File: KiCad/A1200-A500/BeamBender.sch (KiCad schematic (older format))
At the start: 42 parts, among them J1 4-1734742-0, J2 HDMI_A_1.4, J3 STX-3501-3N, J4 Phoenix_Contact, U1 LM1117-3.3, U3 ADV7513BSWZ, X1 Abracon ASE-27.000MHZ-L-R-T

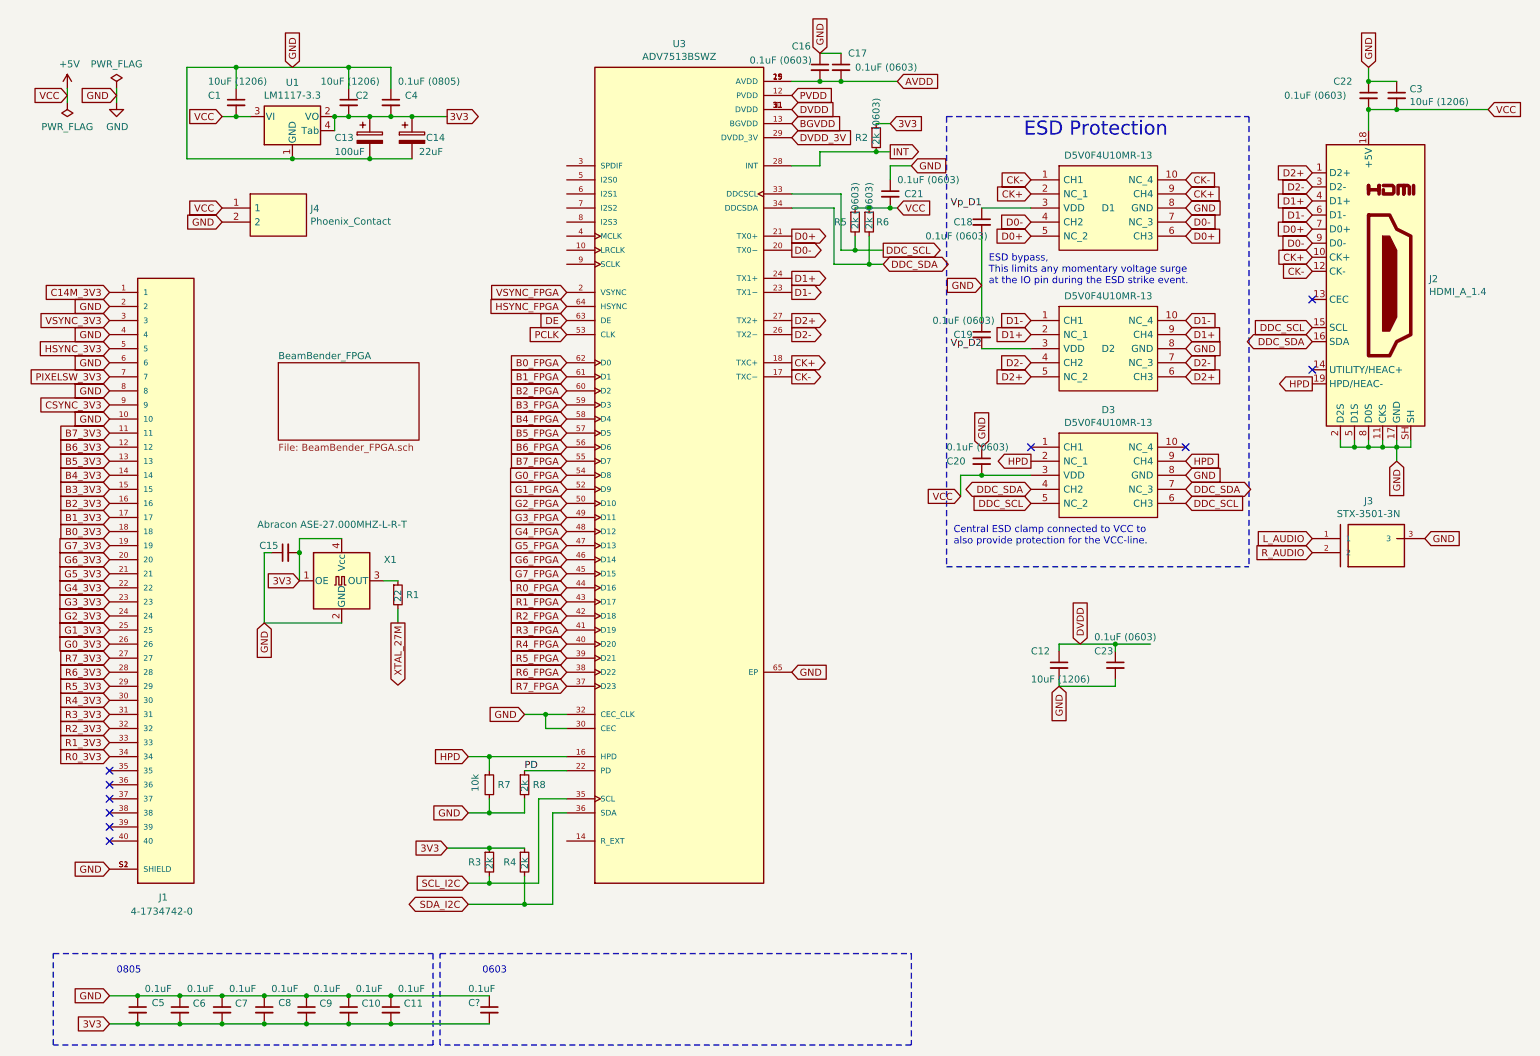
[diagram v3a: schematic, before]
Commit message: Added Oscillator_7.0x5.0mm X2 on GCLKT_1 input and added damping resistor on PCLK
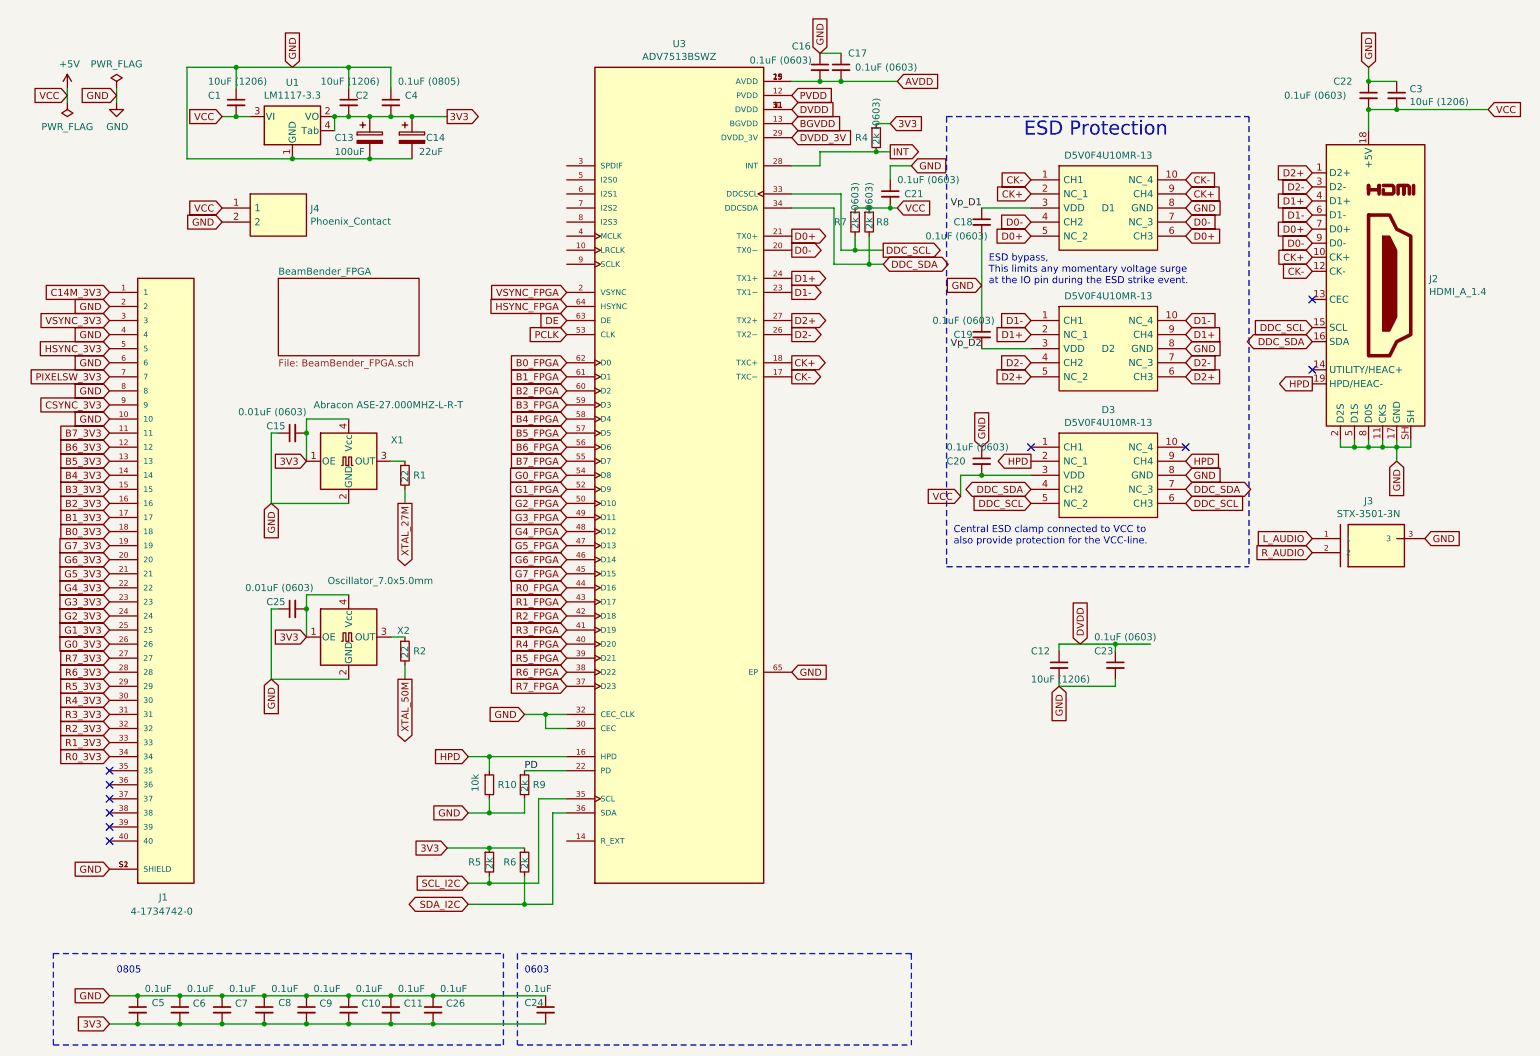
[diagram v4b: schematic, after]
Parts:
- added C25: 0.01uF (0603), Capacitor_SMD:C_0603_1608Metric_Pad1.08x0.95mm_HandSolder, symbol Device:C_Small
- added C26: 0.1uF, Capacitor_SMD:C_0805_2012Metric_Pad1.18x1.45mm_HandSolder, symbol Device:C_Small
- added R2: 22, Resistor_SMD:R_0603_1608Metric_Pad0.98x0.95mm_HandSolder, symbol Device:R_Small
- added X2: Oscillator_7.0x5.0mm, Oscillator:Oscillator_SMD_SeikoEpson_SG8002CA-4Pin_7.0x5.0mm_HandSoldering, symbol Oscillator:SG-8002CA
- C15: value 0.01uF -> 0.01uF (0603)
- C5, C8: footprint Capacitor_SMD:C_0805_2012Metric_Pad1.15x1.40mm_HandSolder -> Capacitor_SMD:C_0805_2012Metric_Pad1.18x1.45mm_HandSolder
- gave numbers to parts that had none: 1
- renumbered R7 to R10, R2 to R4, R3 to R5, R4 to R6, R5 to R7, R6 to R8, R8 to R9
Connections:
- net 3V3: now also C25.2, C26.2, X2.1 (OE), X2.4 (Vcc)
- net GND: now also C25.1, C26.1, X2.2 (GND)
- new net: R2.1, X2.3 (OUT)
- new net XTAL_50M: R2.2
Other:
- moved on the sheet: C15, C24, R1, X1
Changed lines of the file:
@@
 F 0 "C5" H 1450 7550 50  0000 L CNN
 F 1 "0.1uF" H 1400 7650 50  0000 L CNN
-F 2 "Capacitor_SMD:C_0805_2012Metric_Pad1.15x1.40mm_HandSolder" H 1350 7500 50  0001 C CNN
+F 2 "Capacitor_SMD:C_0805_2012Metric_Pad1.18x1.45mm_HandSolder" H 1350 7500 50  0001 C CNN
 F 3 "~" H 1350 7500 50  0001 C CNN
 	1    1350 7500
@@
 F 0 "C8" H 2350 7550 50  0000 L CNN
 F 1 "0.1uF" H 2300 7650 50  0000 L CNN
-F 2 "Capacitor_SMD:C_0805_2012Metric_Pad1.15x1.40mm_HandSolder" H 2250 7500 50  0001 C CNN
+F 2 "Capacitor_SMD:C_0805_2012Metric_Pad1.18x1.45mm_HandSolder" H 2250 7500 50  0001 C CNN
 F 3 "~" H 2250 7500 50  0001 C CNN
 	1    2250 7500
@@
 GND
 $Comp
-L Device:R_Small R5
+L Device:R_Small R7
 U 1 1 6532D8B1
 P 6450 1900
-F 0 "R5" H 6300 1900 50  0000 L CNN
+F 0 "R7" H 6300 1900 50  0000 L CNN
 F 1 "2k  (0603)" V 6450 1850 50  0000 L CNN
 F 2 "Resistor_SMD:R_0603_1608Metric_Pad0.98x0.95mm_HandSolder" H 6450 1900 50  0001 C CNN
@@
 Connection ~ 3000 1450
 $Sheet
-S 2350 2900 1000 550
+S 2350 2300 1000 550
 U 6541C824
 F0 "BeamBender_FPGA" 50
@@
 L Oscillator:SG-8002CE X1
 U 1 1 654B3E8F
-P 2800 4450
-F 0 "X1" H 3100 4600 50  0000 L CNN
-F 1 "Abracon ASE-27.000MHZ-L-R-T" H 2200 4850 50  0000 L CNN
-F 2 "Oscillator:Oscillator_SMD_SeikoEpson_SG8002CE-4Pin_3.2x2.5mm" H 3500 4100 50  0001 C CNN
-F 3 "https://www.mouser.com/datasheet/2/3/ASEseries-1774818.pdf" H 2700 4450 50  0001 C CNN
-	1    2800 4450
-	1    0    0    -1
-$EndComp
-Text GLabel 2250 4750 3    50   Input ~ 0
-GND
-Text GLabel 2500 4450 0    50   Input ~ 0
+P 2850 3600
+F 0 "X1" H 3150 3750 50  0000 L CNN
+F 1 "Abracon ASE-27.000MHZ-L-R-T" H 2600 4000 50  0000 L CNN
+F 2 "Oscillator:Oscillator_SMD_SeikoEpson_SG8002CE-4Pin_3.2x2.5mm" H 3550 3250 50  0001 C CNN
+F 3 "https://www.mouser.com/datasheet/2/3/ASEseries-1774818.pdf" H 2750 3600 50  0001 C CNN
+	1    2850 3600
+	1    0    0    -1
+$EndComp
+Text GLabel 2300 3900 3    50   Input ~ 0
+GND
+Text GLabel 2550 3600 0    50   Input ~ 0
 3V3
 Wire Wire Line
-	2500 4450 2500 4250
-Wire Wire Line
-	2500 4150 2800 4150
+	2550 3600 2550 3400
+Wire Wire Line
+	2550 3300 2850 3300
 $Comp
 L Device:C_Small C15
 U 1 1 654BAF9D
-P 2400 4250
-F 0 "C15" V 2450 4300 50  0000 L CNN
-F 1 "0.01uF" H 2492 4205 50  0001 L CNN
-F 2 "Capacitor_SMD:C_0603_1608Metric_Pad1.08x0.95mm_HandSolder" H 2400 4250 50  0001 C CNN
-F 3 "~" H 2400 4250 50  0001 C CNN
-	1    2400 4250
+P 2450 3400
+F 0 "C15" V 2500 3450 50  0000 L CNN
+F 1 "0.01uF (0603)" V 2600 3300 50  0000 L CNN
+F 2 "Capacitor_SMD:C_0603_1608Metric_Pad1.08x0.95mm_HandSolder" H 2450 3400 50  0001 C CNN
+F 3 "~" H 2450 3400 50  0001 C CNN
+	1    2450 3400
 	0    -1   -1   0
 $EndComp
-Connection ~ 2500 4250
-Wire Wire Line
-	2500 4250 2500 4150
-Wire Wire Line
-	2800 4750 2250 4750
-Wire Wire Line
-	2250 4750 2250 4250
-Wire Wire Line
-	2250 4250 2300 4250
-Text GLabel 3200 4750 3    50   Output ~ 0
+Connection ~ 2550 3400
+Wire Wire Line
+	2550 3400 2550 3300
+Wire Wire Line
+	2850 3900 2300 3900
+Wire Wire Line
+	2300 3900 2300 3400
+Wire Wire Line
+	2300 3400 2350 3400
+Text GLabel 3250 3900 3    50   Output ~ 0
 XTAL_27M
 $Comp
 L Device:R_Small R1
 U 1 1 65512C64
-P 3200 4550
-F 0 "R1" H 3259 4550 50  0000 L CNN
-F 1 "22" V 3200 4500 50  0000 L CNN
-F 2 "Resistor_SMD:R_0603_1608Metric_Pad0.98x0.95mm_HandSolder" H 3200 4550 50  0001 C CNN
-F 3 "~" H 3200 4550 50  0001 C CNN
-	1    3200 4550
-	1    0    0    -1
-$EndComp
-Wire Wire Line
-	3100 4450 3200 4450
-Wire Wire Line
-	3200 4650 3200 4750
+P 3250 3700
+F 0 "R1" H 3309 3700 50  0000 L CNN
+F 1 "22" V 3250 3650 50  0000 L CNN
+F 2 "Resistor_SMD:R_0603_1608Metric_Pad0.98x0.95mm_HandSolder" H 3250 3700 50  0001 C CNN
+F 3 "~" H 3250 3700 50  0001 C CNN
+	1    3250 3700
+	1    0    0    -1
+$EndComp
+Wire Wire Line
+	3150 3600 3250 3600
+Wire Wire Line
+	3250 3800 3250 3900
 Text GLabel 1150 7600 0    50   Input ~ 0
 3V3
@@
 Connection ~ 3300 1150
 $Comp
-L Device:R_Small R6
+L Device:R_Small R8
 U 1 1 6532BC2D
 P 6550 1900
-F 0 "R6" H 6600 1900 50  0000 L CNN
+F 0 "R8" H 6600 1900 50  0000 L CNN
 F 1 "2k  (0603)" V 6550 1850 50  0000 L CNN
 F 2 "Resistor_SMD:R_0603_1608Metric_Pad0.98x0.95mm_HandSolder" H 6550 1900 50  0001 C CNN
@@
 Text Notes 1200 7250 0    50   ~ 0
 0805
-Wire Notes Line
-	750  7100 3450 7100
-Wire Notes Line
-	3450 7100 3450 7750
-Wire Notes Line
-	3450 7750 750  7750
 Wire Notes Line
 	750  7750 750  7100
@@
 	4100 5800 4400 5800
 $Comp
-L Device:R_Small R8
+L Device:R_Small R9
 U 1 1 6531102F
 P 4100 5900
-F 0 "R8" H 4159 5900 50  0000 L CNN
+F 0 "R9" H 4159 5900 50  0000 L CNN
 F 1 "2k" V 4100 5850 50  0000 L CNN
 F 2 "Resistor_SMD:R_0603_1608Metric_Pad0.98x0.95mm_HandSolder" H 4100 5900 50  0001 C CNN
@@
 GND
 $Comp
-L Device:R_Small R7
+L Device:R_Small R10
 U 1 1 652DC9C5
 P 3850 5900
-F 0 "R7" H 3909 5900 50  0000 L CNN
+F 0 "R10" H 3909 5900 50  0000 L CNN
 F 1 "10k" V 3750 5850 50  0000 L CNN
 F 2 "Resistor_SMD:R_0603_1608Metric_Pad0.98x0.95mm_HandSolder" H 3850 5900 50  0001 C CNN
@@
 	4300 6100 4400 6100
 $Comp
-L Device:R_Small R3
+L Device:R_Small R5
 U 1 1 655C6F45
 P 3850 6450
-F 0 "R3" H 3700 6450 50  0000 L CNN
+F 0 "R5" H 3700 6450 50  0000 L CNN
 F 1 "2k" V 3850 6400 50  0000 L CNN
 F 2 "Resistor_SMD:R_0603_1608Metric_Pad0.98x0.95mm_HandSolder" H 3850 6450 50  0001 C CNN
@@
 	3850 6600 4200 6600
 $Comp
-L Device:R_Small R4
+L Device:R_Small R6
 U 1 1 655D3232
 P 4100 6450
-F 0 "R4" H 3950 6450 50  0000 L CNN
+F 0 "R6" H 3950 6450 50  0000 L CNN
 F 1 "2k" V 4100 6400 50  0000 L CNN
 F 2 "Resistor_SMD:R_0603_1608Metric_Pad0.98x0.95mm_HandSolder" H 4100 6450 50  0001 C CNN
@@
 Connection ~ 2250 7600
 Wire Notes Line
-	3500 7100 6850 7100
-Wire Notes Line
 	6850 7100 6850 7750
-Wire Notes Line
-	6850 7750 3500 7750
-Wire Notes Line
-	3500 7750 3500 7100
-Text Notes 3800 7250 0    50   ~ 0
+Text Notes 4100 7250 0    50   ~ 0
 0603
 Wire Wire Line
@@
 PCLK
 $Comp
-L Device:R_Small R2
+L Device:R_Small R4
 U 1 1 656847D2
 P 6600 1300
-F 0 "R2" H 6450 1300 50  0000 L CNN
+F 0 "R4" H 6450 1300 50  0000 L CNN
 F 1 "2k  (0603)" V 6600 1250 50  0000 L CNN
 F 2 "Resistor_SMD:R_0603_1608Metric_Pad0.98x0.95mm_HandSolder" H 6600 1300 50  0001 C CNN
@@
 Connection ~ 3150 7600
 Wire Wire Line
-	3150 7400 3850 7400
-Wire Wire Line
-	3150 7600 3850 7600
+	3150 7400 3450 7400
+Wire Wire Line
+	3150 7600 3450 7600
 $Comp
 L Device:C_Small C17
@@
 	7900 5150 7900 5200
 $Comp
-L Device:C_Small C?
+L Device:C_Small C24
 U 1 1 6584F5FE
-P 3850 7500
-F 0 "C?" H 3700 7550 50  0000 L CNN
-F 1 "0.1uF" H 3700 7650 50  0000 L CNN
-F 2 "Capacitor_SMD:C_0603_1608Metric_Pad1.08x0.95mm_HandSolder" H 3850 7500 50  0001 C CNN
-F 3 "~" H 3850 7500 50  0001 C CNN
-	1    3850 7500
-	1    0    0    -1
-$EndComp
+P 4250 7500
+F 0 "C24" H 4100 7550 50  0000 L CNN
+F 1 "0.1uF" H 4100 7650 50  0000 L CNN
+F 2 "Capacitor_SMD:C_0603_1608Metric_Pad1.08x0.95mm_HandSolder" H 4250 7500 50  0001 C CNN
+F 3 "~" H 4250 7500 50  0001 C CNN
+	1    4250 7500
+	1    0    0    -1
+$EndComp
+$Comp
+L Oscillator:SG-8002CA X2
+U 1 1 658825BB
+P 2850 4850
+F 0 "X2" H 3194 4896 50  0000 L CNN
+F 1 "Oscillator_7.0x5.0mm" H 2700 5250 50  0000 L CNN
+F 2 "Oscillator:Oscillator_SMD_SeikoEpson_SG8002CA-4Pin_7.0x5.0mm_HandSoldering" H 3550 4500 50  0001 C CNN
+F 3 "" H 2750 4850 50  0001 C CNN
+	1    2850 4850
+	1    0    0    -1
+$EndComp
+Text GLabel 2550 4850 0    50   Input ~ 0
+3V3
+Wire Wire Line
+	2850 4550 2550 4550
+Wire Wire Line
+	2550 4550 2550 4650
+$Comp
+L Device:R_Small R2
+U 1 1 6589F17E
+P 3250 4950
+F 0 "R2" H 3309 4950 50  0000 L CNN
+F 1 "22" V 3250 4900 50  0000 L CNN
+F 2 "Resistor_SMD:R_0603_1608Metric_Pad0.98x0.95mm_HandSolder" H 3250 4950 50  0001 C CNN
+F 3 "~" H 3250 4950 50  0001 C CNN
+	1    3250 4950
+	1    0    0    -1
+$EndComp
+Wire Wire Line
+	3250 5050 3250 5150
+Wire Wire Line
+	3150 4850 3250 4850
+Text GLabel 3250 5150 3    50   Output ~ 0
+XTAL_50M
+$Comp
+L Device:C_Small C25
+U 1 1 658AB783
+P 2450 4650
+F 0 "C25" V 2500 4700 50  0000 L CNN
+F 1 "0.01uF (0603)" V 2600 4500 50  0000 L CNN
+F 2 "Capacitor_SMD:C_0603_1608Metric_Pad1.08x0.95mm_HandSolder" H 2450 4650 50  0001 C CNN
+F 3 "~" H 2450 4650 50  0001 C CNN
+	1    2450 4650
+	0    -1   -1   0
+$EndComp
+Connection ~ 2550 4650
+Wire Wire Line
+	2550 4650 2550 4850
+Text GLabel 2300 5150 3    50   Input ~ 0
+GND
+Wire Wire Line
+	2850 5150 2300 5150
+Wire Wire Line
+	2300 5150 2300 4650
+Wire Wire Line
+	2300 4650 2350 4650
+$Comp
+L Device:C_Small C26
+U 1 1 6591CDE3
+P 3450 7500
+F 0 "C26" H 3542 7546 50  0000 L CNN
+F 1 "0.1uF" H 3500 7650 50  0000 L CNN
+F 2 "Capacitor_SMD:C_0805_2012Metric_Pad1.18x1.45mm_HandSolder" H 3450 7500 50  0001 C CNN
+F 3 "~" H 3450 7500 50  0001 C CNN
+	1    3450 7500
+	1    0    0    -1
+$EndComp
+Connection ~ 3450 7400
+Connection ~ 3450 7600
+Wire Notes Line
+	3950 7750 3950 7100
+Wire Notes Line
+	750  7100 3950 7100
+Wire Notes Line
+	750  7750 3950 7750
+Wire Wire Line
+	3450 7400 4250 7400
+Wire Wire Line
+	3450 7600 4250 7600
+Wire Notes Line
+	4050 7100 4050 7750
+Wire Notes Line
+	4050 7750 6850 7750
+Wire Notes Line
+	6850 7100 4050 7100
 $EndSCHEMATC
